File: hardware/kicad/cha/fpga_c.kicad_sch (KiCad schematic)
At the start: 33 parts, among them J2 PROG C, U12 iCE40HX4K-TQ144, U13 W25Q32JVSS, X1 25 MHz 3,3 V

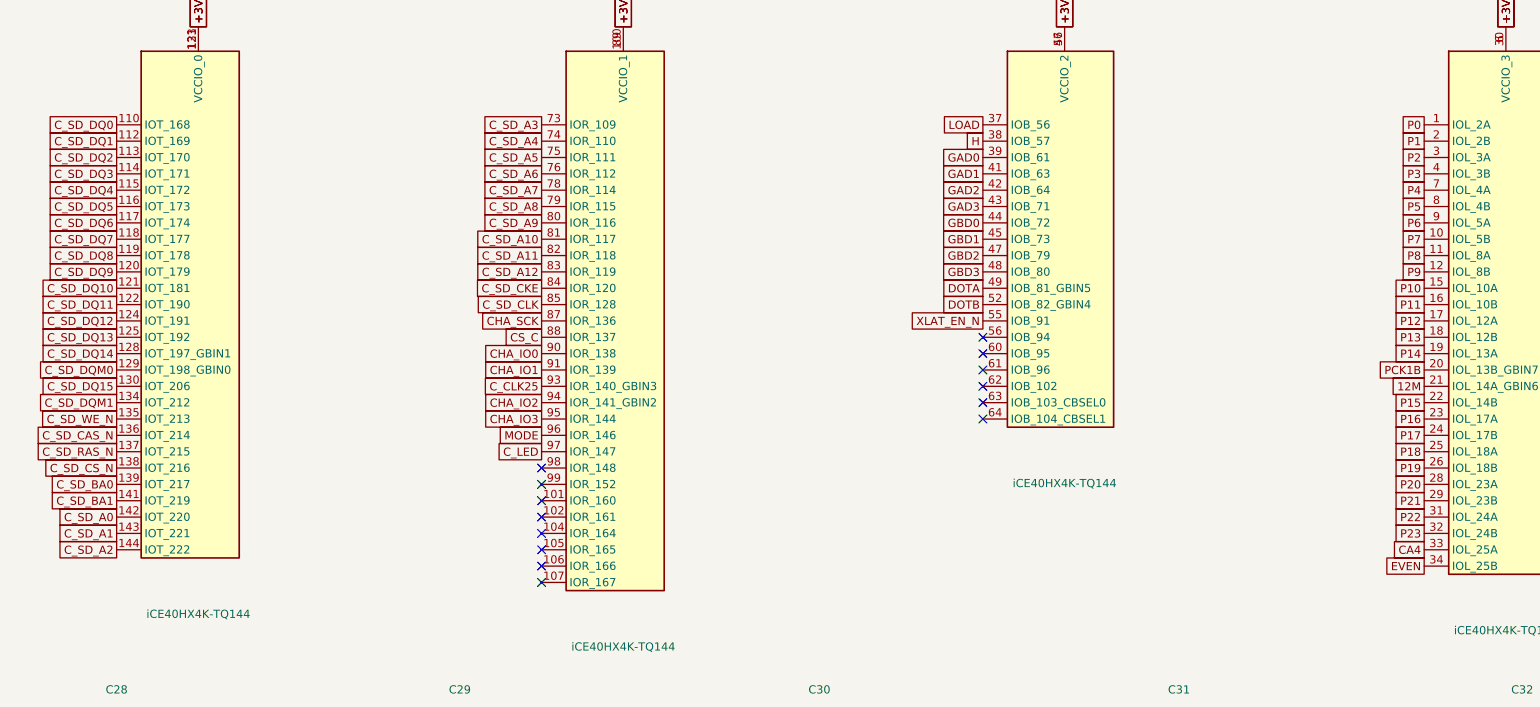
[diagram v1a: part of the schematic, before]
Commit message: Circuits imprimés 2 couches : placement et affectation des broches FPGA
- hardware/gen/pcb.py : empreintes et réseaux depuis boards.py, contour
  depuis outline.py ; ancres placées (contacts, rangée de tampons, FPGA,
  mémoires ; CHA : Pico au centre, microSD et bouton en haut), passifs
  au plus près de leur broche, masse coulée sur les deux faces.
- --pins : signaux des FPGA affectés aux broches tournées vers leur
  cible en conservant l'ordre circulaire (pins_opt.json, repris par
  fpga_pins.py) ; stable en trois passes.
- boards.py : canaux des tampons triés selon la position des contacts.
- hardware/gen/route.py : export Specctra, Freerouting, relecture de la
  session, DRC.
Placement-routage FPGA avec les nouvelles broches : en cours de
vérification.

Co-Authored-By: Claude Opus 5.5 <noreply@anthropic.com>
Claude-Session: https://claude.ai/code/session_01WKfXP1YJ8otGxZ5dsY6Agh
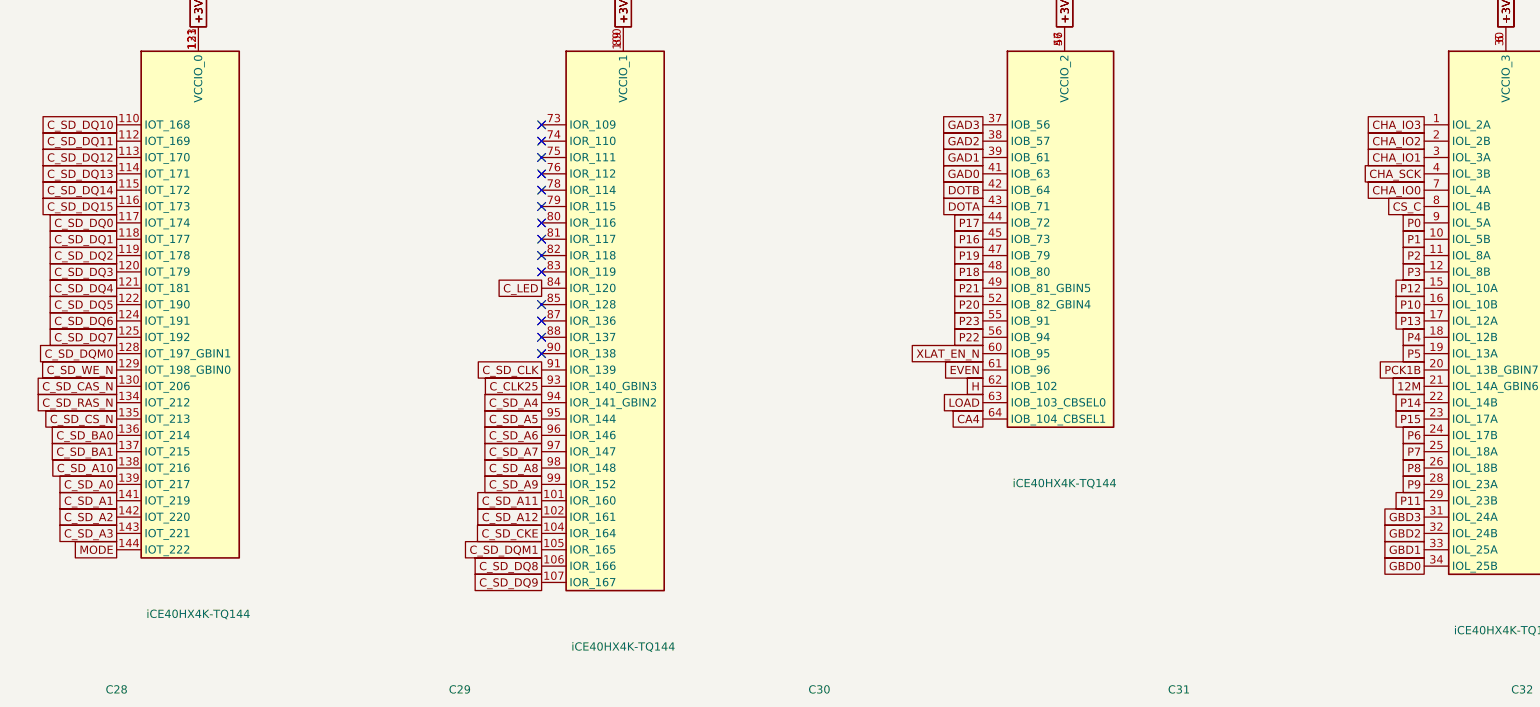
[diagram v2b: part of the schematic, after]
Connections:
- net CA4: now also U12.64 (IOB_104_CBSEL1); no longer U12.33 (IOL_25A)
- net CHA_IO0: now also U12.7 (IOL_4A); no longer U12.90 (IOR_138)
- net CHA_IO1: now also U12.3 (IOL_3A); no longer U12.91 (IOR_139)
- net CHA_IO2: now also U12.2 (IOL_2B); no longer U12.94 (IOR_141_GBIN2)
- net CHA_IO3: now also U12.1 (IOL_2A); no longer U12.95 (IOR_144)
- net CHA_SCK: now also U12.4 (IOL_3B); no longer U12.87 (IOR_136)
- net CS_C: now also U12.8 (IOL_4B); no longer U12.88 (IOR_137)
- net C_LED: now also U12.84 (IOR_120); no longer U12.97 (IOR_147)
- net C_SD_A0: now also U12.139 (IOT_217); no longer U12.142 (IOT_220)
- net C_SD_A1: now also U12.141 (IOT_219); no longer U12.143 (IOT_221)
- net C_SD_A10: now also U12.138 (IOT_216); no longer U12.81 (IOR_117)
- net C_SD_A11: now also U12.101 (IOR_160); no longer U12.82 (IOR_118)
- net C_SD_A12: now also U12.102 (IOR_161); no longer U12.83 (IOR_119)
- net C_SD_A2: now also U12.142 (IOT_220); no longer U12.144 (IOT_222)
- net C_SD_A3: now also U12.143 (IOT_221); no longer U12.73 (IOR_109)
- net C_SD_A4: now also U12.94 (IOR_141_GBIN2); no longer U12.74 (IOR_110)
- net C_SD_A5: now also U12.95 (IOR_144); no longer U12.75 (IOR_111)
- net C_SD_A6: now also U12.96 (IOR_146); no longer U12.76 (IOR_112)
- net C_SD_A7: now also U12.97 (IOR_147); no longer U12.78 (IOR_114)
- net C_SD_A8: now also U12.98 (IOR_148); no longer U12.79 (IOR_115)
- net C_SD_A9: now also U12.99 (IOR_152); no longer U12.80 (IOR_116)
- net C_SD_BA0: now also U12.136 (IOT_214); no longer U12.139 (IOT_217)
- net C_SD_BA1: now also U12.137 (IOT_215); no longer U12.141 (IOT_219)
- net C_SD_CAS_N: now also U12.130 (IOT_206); no longer U12.136 (IOT_214)
- net C_SD_CKE: now also U12.104 (IOR_164); no longer U12.84 (IOR_120)
- net C_SD_CLK: now also U12.91 (IOR_139); no longer U12.85 (IOR_128)
- net C_SD_CS_N: now also U12.135 (IOT_213); no longer U12.138 (IOT_216)
- net C_SD_DQ0: now also U12.117 (IOT_174); no longer U12.110 (IOT_168)
- net C_SD_DQ1: now also U12.118 (IOT_177); no longer U12.112 (IOT_169)
- net C_SD_DQ10: now also U12.110 (IOT_168); no longer U12.121 (IOT_181)
- net C_SD_DQ11: now also U12.112 (IOT_169); no longer U12.122 (IOT_190)
- net C_SD_DQ12: now also U12.113 (IOT_170); no longer U12.124 (IOT_191)
- net C_SD_DQ13: now also U12.114 (IOT_171); no longer U12.125 (IOT_192)
- net C_SD_DQ14: now also U12.115 (IOT_172); no longer U12.128 (IOT_197_GBIN1)
- net C_SD_DQ15: now also U12.116 (IOT_173); no longer U12.130 (IOT_206)
- net C_SD_DQ2: now also U12.119 (IOT_178); no longer U12.113 (IOT_170)
- net C_SD_DQ3: now also U12.120 (IOT_179); no longer U12.114 (IOT_171)
- net C_SD_DQ4: now also U12.121 (IOT_181); no longer U12.115 (IOT_172)
- net C_SD_DQ5: now also U12.122 (IOT_190); no longer U12.116 (IOT_173)
- net C_SD_DQ6: now also U12.124 (IOT_191); no longer U12.117 (IOT_174)
- net C_SD_DQ7: now also U12.125 (IOT_192); no longer U12.118 (IOT_177)
- net C_SD_DQ8: now also U12.106 (IOR_166); no longer U12.119 (IOT_178)
- net C_SD_DQ9: now also U12.107 (IOR_167); no longer U12.120 (IOT_179)
- net C_SD_DQM0: now also U12.128 (IOT_197_GBIN1); no longer U12.129 (IOT_198_GBIN0)
- net C_SD_DQM1: now also U12.105 (IOR_165); no longer U12.134 (IOT_212)
- net C_SD_RAS_N: now also U12.134 (IOT_212); no longer U12.137 (IOT_215)
- net C_SD_WE_N: now also U12.129 (IOT_198_GBIN0); no longer U12.135 (IOT_213)
- net DOTA: now also U12.43 (IOB_71); no longer U12.49 (IOB_81_GBIN5)
- net DOTB: now also U12.42 (IOB_64); no longer U12.52 (IOB_82_GBIN4)
- net EVEN: now also U12.61 (IOB_96); no longer U12.34 (IOL_25B)
- net GAD0: now also U12.41 (IOB_63); no longer U12.39 (IOB_61)
- net GAD1: now also U12.39 (IOB_61); no longer U12.41 (IOB_63)
- net GAD2: now also U12.38 (IOB_57); no longer U12.42 (IOB_64)
- net GAD3: now also U12.37 (IOB_56); no longer U12.43 (IOB_71)
- net GBD0: now also U12.34 (IOL_25B); no longer U12.44 (IOB_72)
- net GBD1: now also U12.33 (IOL_25A); no longer U12.45 (IOB_73)
- net GBD2: now also U12.32 (IOL_24B); no longer U12.47 (IOB_79)
- net GBD3: now also U12.31 (IOL_24A); no longer U12.48 (IOB_80)
- net H: now also U12.62 (IOB_102); no longer U12.38 (IOB_57)
- net LOAD: now also U12.63 (IOB_103_CBSEL0); no longer U12.37 (IOB_56)
- net MODE: now also U12.144 (IOT_222); no longer U12.96 (IOR_146)
- net P0: now also U12.9 (IOL_5A); no longer U12.1 (IOL_2A)
- net P1: now also U12.10 (IOL_5B); no longer U12.2 (IOL_2B)
- net P10: now also U12.16 (IOL_10B); no longer U12.15 (IOL_10A)
- net P11: now also U12.29 (IOL_23B); no longer U12.16 (IOL_10B)
- net P12: now also U12.15 (IOL_10A); no longer U12.17 (IOL_12A)
- net P13: now also U12.17 (IOL_12A); no longer U12.18 (IOL_12B)
- net P14: now also U12.22 (IOL_14B); no longer U12.19 (IOL_13A)
- net P15: now also U12.23 (IOL_17A); no longer U12.22 (IOL_14B)
- net P16: now also U12.45 (IOB_73); no longer U12.23 (IOL_17A)
- net P17: now also U12.44 (IOB_72); no longer U12.24 (IOL_17B)
- net P18: now also U12.48 (IOB_80); no longer U12.25 (IOL_18A)
- net P19: now also U12.47 (IOB_79); no longer U12.26 (IOL_18B)
- net P2: now also U12.11 (IOL_8A); no longer U12.3 (IOL_3A)
- net P20: now also U12.52 (IOB_82_GBIN4); no longer U12.28 (IOL_23A)
- net P21: now also U12.49 (IOB_81_GBIN5); no longer U12.29 (IOL_23B)
- net P22: now also U12.56 (IOB_94); no longer U12.31 (IOL_24A)
- net P23: now also U12.55 (IOB_91); no longer U12.32 (IOL_24B)
- net P3: now also U12.12 (IOL_8B); no longer U12.4 (IOL_3B)
- net P4: now also U12.18 (IOL_12B); no longer U12.7 (IOL_4A)
- net P5: now also U12.19 (IOL_13A); no longer U12.8 (IOL_4B)
- net P6: now also U12.24 (IOL_17B); no longer U12.9 (IOL_5A)
- net P7: now also U12.25 (IOL_18A); no longer U12.10 (IOL_5B)
- net P8: now also U12.26 (IOL_18B); no longer U12.11 (IOL_8A)
- net P9: now also U12.28 (IOL_23A); no longer U12.12 (IOL_8B)
- net XLAT_EN_N: now also U12.60 (IOB_95); no longer U12.55 (IOB_91)

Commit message: FPGA configurés par le RP2350 depuis la carte SD (plus de flash)
- Matériel : flash SPI retirées (4 W25Q32, 12 résistances, 4
  condensateurs). Le bus de liaison arrive sur les broches de
  configuration des iCE40 (LK_SCK -> 70 SCK, LK_IO[0] -> 68 SDI,
  LK_CS_N -> 71 SS), qui redeviennent ces entrées après le démarrage.
  CRESET_N commun aux 4 FPGA, tiré à la masse, piloté par le RP2350
  (GP28) ; câble PROG-CHA en 2 x 7 (CRESET_N + masse). Connecteur 2 x 3
  de secours par FPGA (iceprog -S).
- Firmware : fpga_boot.c (reset commun en mode SPI esclave, envoi des
  SDAES/fpga_*.bin l'un après l'autre, contrôle de CDONE) ; testé sur
  PC (bitstreams reçus à l'identique, FPGA laissés en reset si un
  fichier manque).
- make -C hdl sd : fichiers à copier sur la carte SD.
- PCB : table de placement et références des FPGA mises à jour,
  broches réoptimisées.
Placement-routage des FPGA avec les nouvelles broches : en cours.

Co-Authored-By: Claude Opus 5.5 <noreply@anthropic.com>
Claude-Session: https://claude.ai/code/session_01WKfXP1YJ8otGxZ5dsY6Agh
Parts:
- removed C42: 100n, Capacitor_SMD:C_0603_1608Metric, symbol Device:C
- removed R10, R9: 10k, Resistor_SMD:R_0603_1608Metric, symbol Device:R
- removed R11: 470, Resistor_SMD:R_0603_1608Metric, symbol Device:R
- removed U13: W25Q32JVSS, Package_SO:SOIC-8_5.23x5.23mm_P1.27mm, symbol Memory_Flash:W25Q32JVSS
- J2: value PROG C -> CONF C
- R8: value 10k -> 470
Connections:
- net C_FL_DO is gone; now on net CHA_IO0: J2.4 (Pin_4), U12.68 (IOB_106_SDI)
- net C_FL_SCK is gone; now on net CHA_SCK: J2.1 (Pin_1), U12.70 (IOB_107_SCK)
- net +3V3: no longer R7.1, R8.1
- net CA4: now also U12.62 (IOB_102); no longer U12.64 (IOB_104_CBSEL1)
- net CHA_IO0: no longer U12.7 (IOL_4A)
- net CHA_IO1: now also U12.4 (IOL_3B); no longer U12.3 (IOL_3A)
- net CHA_IO2: now also U12.3 (IOL_3A); no longer U12.2 (IOL_2B)
- net CHA_IO3: now also U12.2 (IOL_2B); no longer U12.1 (IOL_2A)
- net CHA_SCK: no longer U12.4 (IOL_3B)
- net CS_C: now also J2.2 (Pin_2), U12.71 (IOB_108_SS); no longer U12.8 (IOL_4B)
- net C_LED: now also R8.1, U12.87 (IOR_136); no longer U12.84 (IOR_120)
- net C_LED_K: now also R8.2
- net C_SD_A0: now also U12.141 (IOT_219); no longer U12.139 (IOT_217)
- net C_SD_A1: now also U12.142 (IOT_220); no longer U12.141 (IOT_219)
- net C_SD_A10: now also U12.139 (IOT_217); no longer U12.138 (IOT_216)
- net C_SD_A11: now also U12.102 (IOR_161); no longer U12.101 (IOR_160)
- net C_SD_A12: now also U12.104 (IOR_164); no longer U12.102 (IOR_161)
- net C_SD_A2: now also U12.143 (IOT_221); no longer U12.142 (IOT_220)
- net C_SD_A3: now also U12.144 (IOT_222); no longer U12.143 (IOT_221)
- net C_SD_A4: now also U12.95 (IOR_144); no longer U12.94 (IOR_141_GBIN2)
- net C_SD_A5: now also U12.96 (IOR_146); no longer U12.95 (IOR_144)
- net C_SD_A6: now also U12.97 (IOR_147); no longer U12.96 (IOR_146)
- net C_SD_A7: now also U12.98 (IOR_148); no longer U12.97 (IOR_147)
- net C_SD_A8: now also U12.99 (IOR_152); no longer U12.98 (IOR_148)
- net C_SD_A9: now also U12.101 (IOR_160); no longer U12.99 (IOR_152)
- net C_SD_BA0: now also U12.137 (IOT_215); no longer U12.136 (IOT_214)
- net C_SD_BA1: now also U12.138 (IOT_216); no longer U12.137 (IOT_215)
- net C_SD_CAS_N: now also U12.134 (IOT_212); no longer U12.130 (IOT_206)
- net C_SD_CKE: now also U12.105 (IOR_165); no longer U12.104 (IOR_164)
- net C_SD_CLK: now also U12.94 (IOR_141_GBIN2); no longer U12.91 (IOR_139)
- net C_SD_CS_N: now also U12.136 (IOT_214); no longer U12.135 (IOT_213)
- net C_SD_DQ0: now also U12.118 (IOT_177); no longer U12.117 (IOT_174)
- net C_SD_DQ1: now also U12.119 (IOT_178); no longer U12.118 (IOT_177)
- net C_SD_DQ10: now also U12.112 (IOT_169); no longer U12.110 (IOT_168)
- net C_SD_DQ11: now also U12.113 (IOT_170); no longer U12.112 (IOT_169)
- net C_SD_DQ12: now also U12.114 (IOT_171); no longer U12.113 (IOT_170)
- net C_SD_DQ13: now also U12.115 (IOT_172); no longer U12.114 (IOT_171)
- net C_SD_DQ14: now also U12.116 (IOT_173); no longer U12.115 (IOT_172)
- net C_SD_DQ15: now also U12.117 (IOT_174); no longer U12.116 (IOT_173)
- net C_SD_DQ2: now also U12.120 (IOT_179); no longer U12.119 (IOT_178)
- net C_SD_DQ3: now also U12.121 (IOT_181); no longer U12.120 (IOT_179)
- net C_SD_DQ4: now also U12.122 (IOT_190); no longer U12.121 (IOT_181)
- net C_SD_DQ5: now also U12.124 (IOT_191); no longer U12.122 (IOT_190)
- net C_SD_DQ6: now also U12.125 (IOT_192); no longer U12.124 (IOT_191)
- net C_SD_DQ7: now also U12.128 (IOT_197_GBIN1); no longer U12.125 (IOT_192)
- net C_SD_DQ8: now also U12.107 (IOR_167); no longer U12.106 (IOR_166)
- net C_SD_DQ9: now also U12.110 (IOT_168); no longer U12.107 (IOR_167)
- net C_SD_DQM0: now also U12.129 (IOT_198_GBIN0); no longer U12.128 (IOT_197_GBIN1)
- net C_SD_DQM1: now also U12.106 (IOR_166); no longer U12.105 (IOR_165)
- net C_SD_RAS_N: now also U12.135 (IOT_213); no longer U12.134 (IOT_212)
- net C_SD_WE_N: now also U12.130 (IOT_206); no longer U12.129 (IOT_198_GBIN0)
- net DOTA: now also U12.41 (IOB_63); no longer U12.43 (IOB_71)
- net DOTB: now also U12.39 (IOB_61); no longer U12.42 (IOB_64)
- net EVEN: now also U12.56 (IOB_94); no longer U12.61 (IOB_96)
- net GAD0: now also U12.38 (IOB_57); no longer U12.41 (IOB_63)
- net GAD1: now also U12.37 (IOB_56); no longer U12.39 (IOB_61)
- net GAD2: now also U12.34 (IOL_25B); no longer U12.38 (IOB_57)
- net GAD3: now also U12.33 (IOL_25A); no longer U12.37 (IOB_56)
- net GBD0: now also U12.32 (IOL_24B); no longer U12.34 (IOL_25B)
- net GBD1: now also U12.31 (IOL_24A); no longer U12.33 (IOL_25A)
- net GBD2: now also U12.29 (IOL_23B); no longer U12.32 (IOL_24B)
- net GBD3: now also U12.28 (IOL_23A); no longer U12.31 (IOL_24A)
- net GND: now also R7.2
- net H: now also U12.60 (IOB_95); no longer U12.62 (IOB_102)
- net LOAD: now also U12.61 (IOB_96); no longer U12.63 (IOB_103_CBSEL0)
- net MODE: now also U12.1 (IOL_2A); no longer U12.144 (IOT_222)
- net P0: now also U12.7 (IOL_4A); no longer U12.9 (IOL_5A)
- net P1: now also U12.8 (IOL_4B); no longer U12.10 (IOL_5B)
- net P10: now also U12.9 (IOL_5A); no longer U12.16 (IOL_10B)
- net P11: now also U12.26 (IOL_18B); no longer U12.29 (IOL_23B)
- net P12: now also U12.12 (IOL_8B); no longer U12.15 (IOL_10A)
- net P13: now also U12.15 (IOL_10A); no longer U12.17 (IOL_12A)
- net P14: now also U12.18 (IOL_12B); no longer U12.22 (IOL_14B)
- net P15: now also U12.19 (IOL_13A); no longer U12.23 (IOL_17A)
- net P16: now also U12.43 (IOB_71); no longer U12.45 (IOB_73)
- net P17: now also U12.42 (IOB_64); no longer U12.44 (IOB_72)
- net P18: now also U12.45 (IOB_73); no longer U12.48 (IOB_80)
- net P19: now also U12.44 (IOB_72); no longer U12.47 (IOB_79)
- net P2: now also U12.10 (IOL_5B); no longer U12.11 (IOL_8A)
- net P20: now also U12.48 (IOB_80); no longer U12.52 (IOB_82_GBIN4)
- net P21: now also U12.47 (IOB_79); no longer U12.49 (IOB_81_GBIN5)
- net P22: now also U12.52 (IOB_82_GBIN4); no longer U12.56 (IOB_94)
- net P23: now also U12.49 (IOB_81_GBIN5); no longer U12.55 (IOB_91)
- net P3: now also U12.11 (IOL_8A); no longer U12.12 (IOL_8B)
- net P4: now also U12.16 (IOL_10B); no longer U12.18 (IOL_12B)
- net P5: now also U12.17 (IOL_12A); no longer U12.19 (IOL_13A)
- net P6: now also U12.22 (IOL_14B); no longer U12.24 (IOL_17B)
- net P7: now also U12.24 (IOL_17B); no longer U12.25 (IOL_18A)
- net P8: now also U12.23 (IOL_17A); no longer U12.26 (IOL_18B)
- net P9: now also U12.25 (IOL_18A); no longer U12.28 (IOL_23A)
- net XLAT_EN_N: now also U12.55 (IOB_91); no longer U12.60 (IOB_95)
- net C_CRESET_N renamed CRESET_N
- net CRESET_N: now also R7.1; no longer R7.2
- removed net C_FL_CS_N: J2.2 (Pin_2), R8.2, U12.71 (IOB_108_SS)
- net C_FL_DI renamed C_SDO
- no-connect marks 22 -> 25
